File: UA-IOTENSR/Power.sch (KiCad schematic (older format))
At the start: 29 parts, among them J201 ZX62-AB-5PA_31_, J202 S2B-ZR-SM4A-TF(LF)(SN), Q201 2N7002, U201 BQ24196RGER, U202 BD33KA5FP-E2

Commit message: Adding peripherals page
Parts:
- renumbered C211 to C201, C201 to C202, C202 to C203, C212 to C204, C203 to C205, C204 to C206, C205 to C207, C206 to C208, C207 to C209, C208 to C210, C209 to C211, C210 to C212, R207 to R205, R208 to R206, R206 to R207, R205 to R208, U202 to U201, U201 to U202
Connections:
- net labels removed: NoConn
- no-connect marks 0 -> 2
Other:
- moved on the sheet: C201, C202, C203, C204, C205, C206, C207, C208, C209, C210, C211, C212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

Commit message: updated symbols; changed vdd to 3v3 global for pcb design later
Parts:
- removed R202: 10k, symbol Device:R_Small_US
- added R2: 10k, symbol Device:R_Small_US
- D1: renamed from D201; symbol Samacs:PRTR5V0U2X,215 -> UA-IOTENSR-rescue:PRTR5V0U2X,215-Samacs
- J1: renamed from J201; symbol Samacs:ZX62-AB-5PA_31_ -> UA-IOTENSR-rescue:ZX62-AB-5PA_31_-Samacs
- renumbered C201 to C1, C210 to C10, C211 to C11, C212 to C12, C202 to C2, C203 to C3, C204 to C4, C205 to C5, C206 to C6, C207 to C7, C208 to C8, C209 to C9, D202 to D2, D203 to D3, J202 to J2, L201 to L1, Q201 to Q1, R201 to R1, R203 to R3, R204 to R4, R205 to R5, R206 to R6, R207 to R7, R208 to R8, U201 to U2, U202 to U3
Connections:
- net labels added: +5V
- net labels removed: VDD
- wire segments 91 -> 97
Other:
- moved on the sheet: C10

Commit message: Organized PMIC schem
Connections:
- wire segments 97 -> 101
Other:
- note added: "BQ24196 PMIC BATTERY CHARGING CCT"
- note added: "MicroUSB HEADER and TVS DIODE ARRAY IC"
- moved on the sheet: C1, C10, C11, C12, C2, C3, C4, C5, C6, C7, C8, C9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

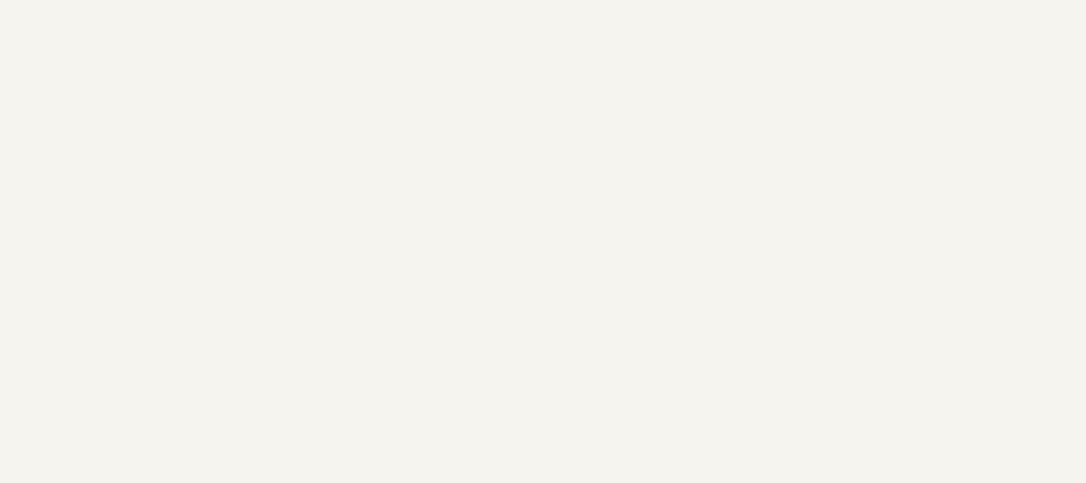
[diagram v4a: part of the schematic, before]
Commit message: Organized ESP32 main schem
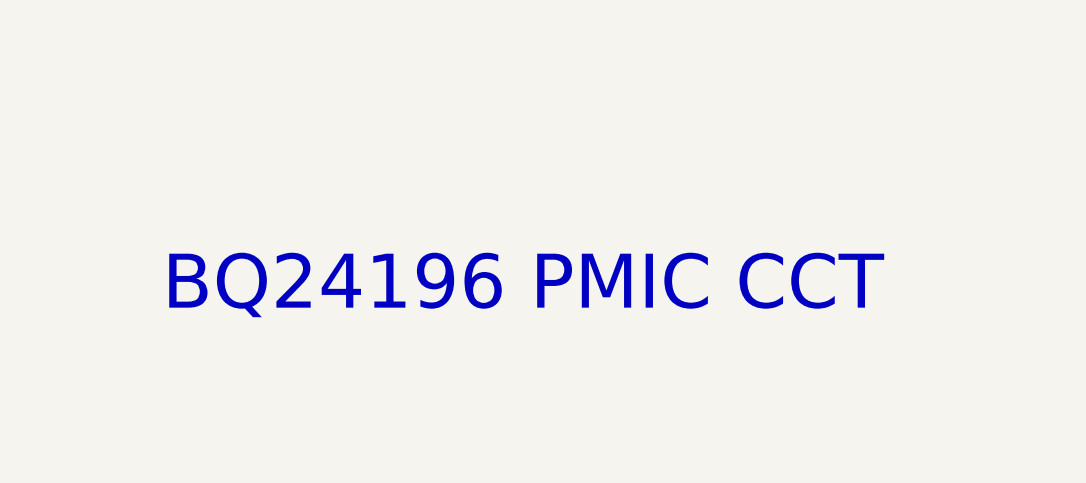
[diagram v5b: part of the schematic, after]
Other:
- note added: "BQ24196 PMIC CCT"
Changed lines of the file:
@@
 Text Notes 6450 5200 0    118  ~ 0
 BQ24196 PMIC BATTERY CHARGING CCT
+Text Notes 7000 7100 0    236  ~ 0
+BQ24196 PMIC CCT
 $EndSCHEMATC

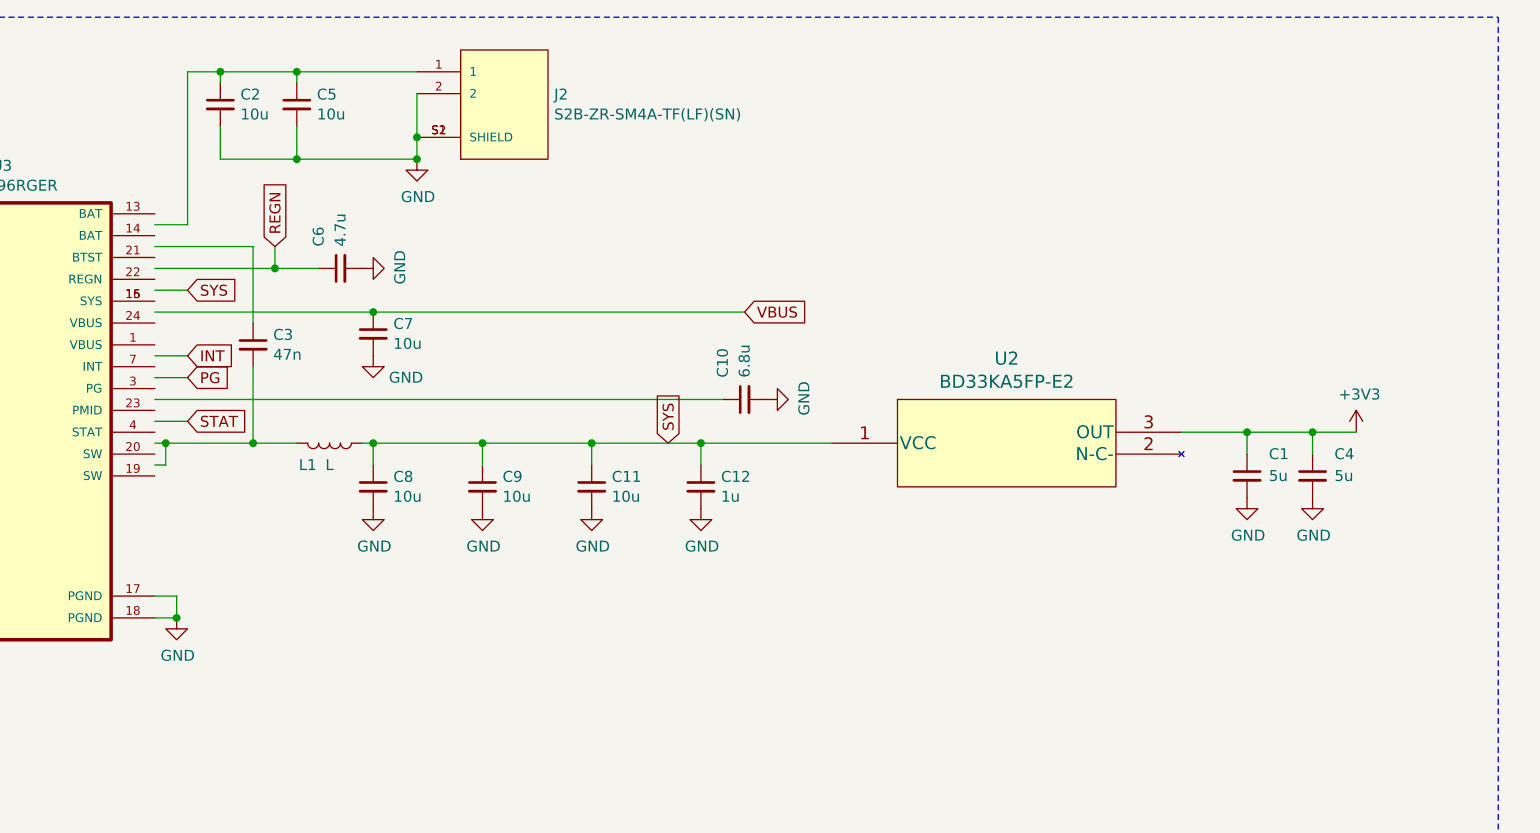
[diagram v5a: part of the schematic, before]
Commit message: Reassessed components
Removed bar graph led array and lm3914
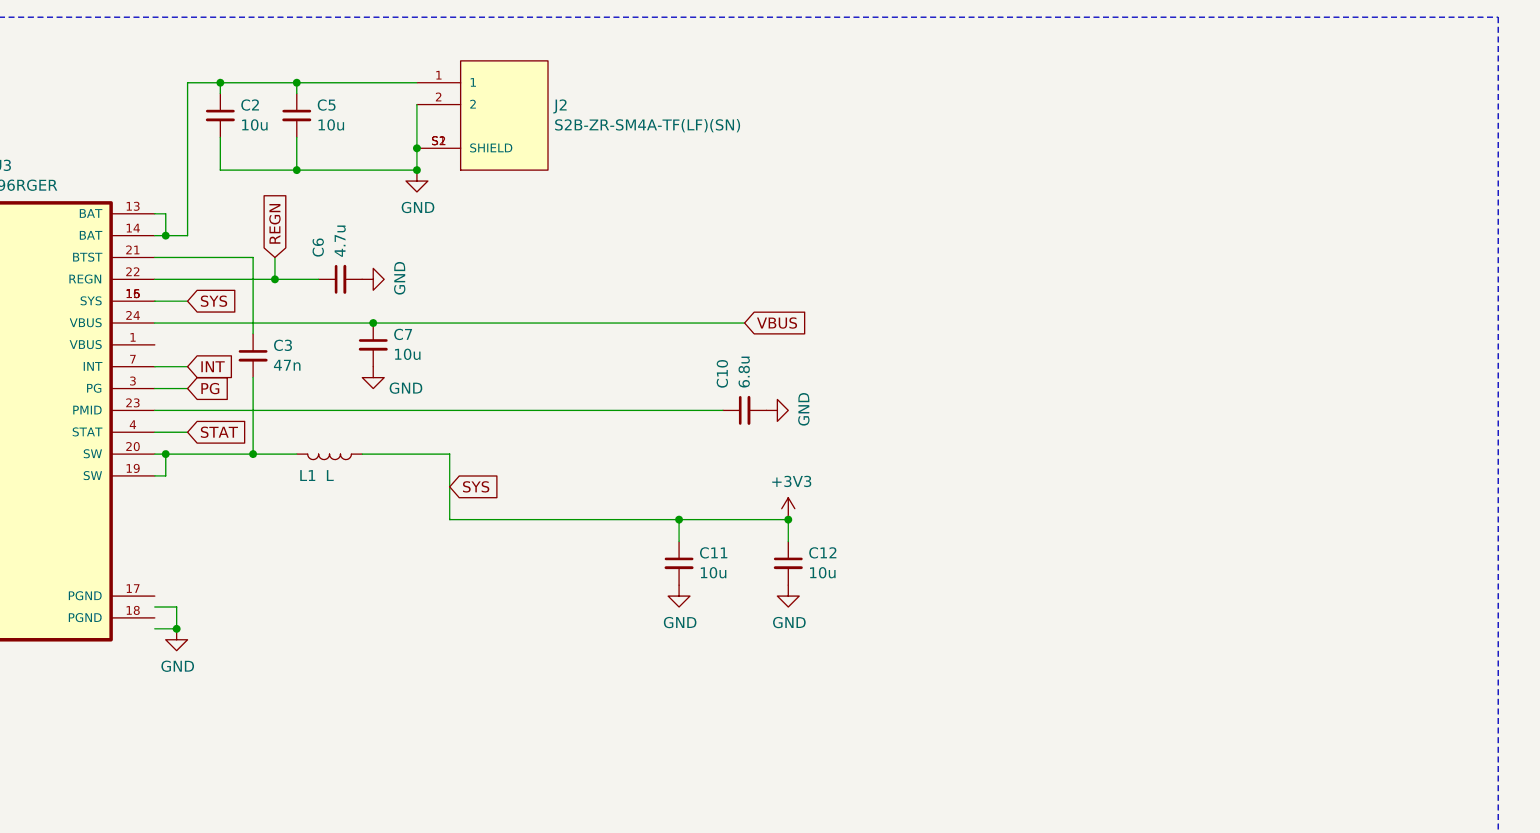
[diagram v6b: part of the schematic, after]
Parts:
- removed C1, C4: 5u, symbol Device:C_Small
- removed C8, C9: 10u, symbol Device:C_Small
- removed U2: BD33KA5FP-E2, TO252-3_ROM, symbol VoltReg:BD33KA5FP-E2
- C12: value 1u -> 10u
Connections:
- wire segments 101 -> 96
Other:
- moved on the sheet: C10, C11, C12, C2, C3, C5, C6, C7, J2, L1

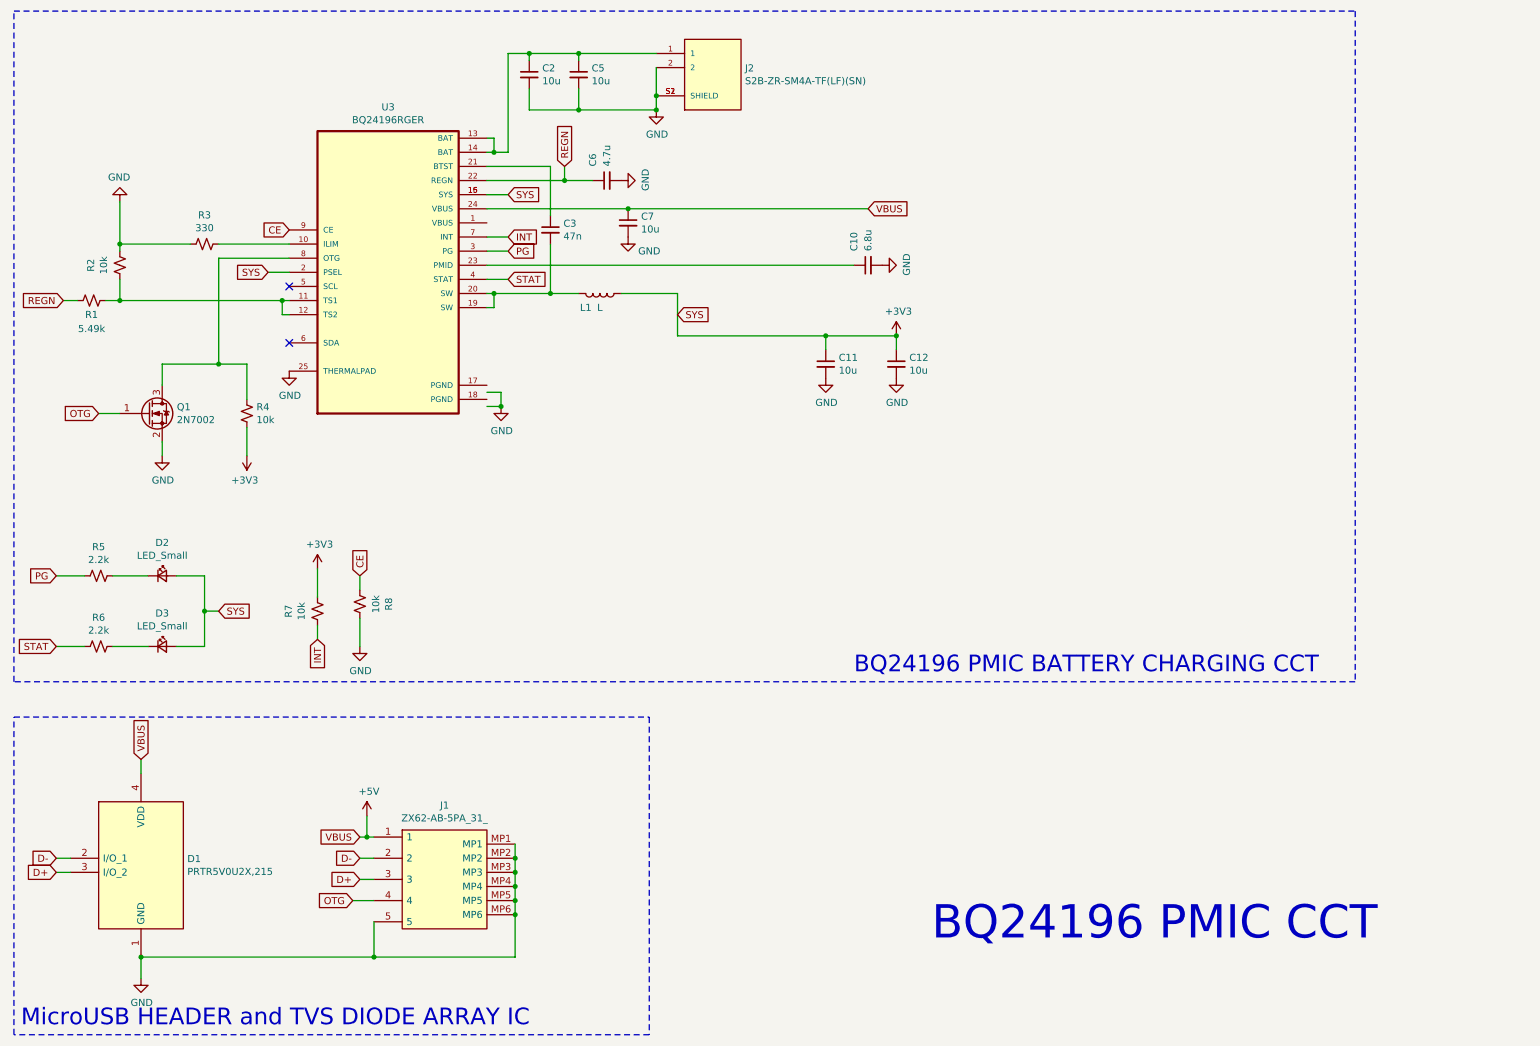
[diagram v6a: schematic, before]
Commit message: Reworking Power Schematic page for the change to NiMH tech
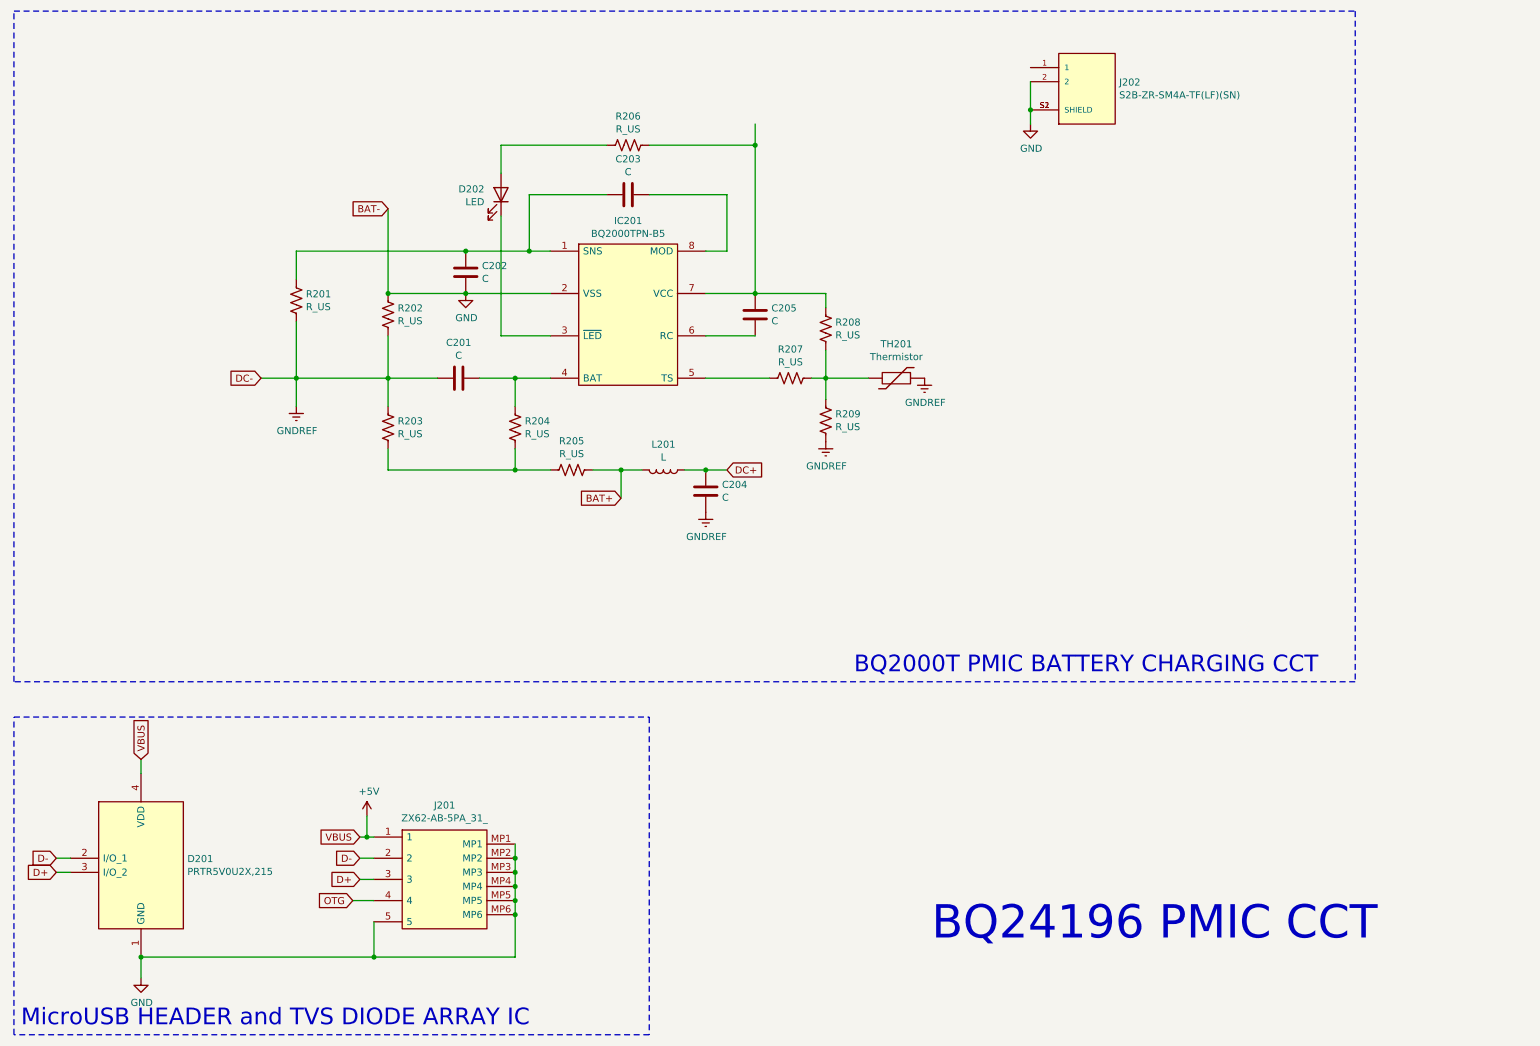
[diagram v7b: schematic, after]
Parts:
- removed C10: 6.8u, symbol Device:C_Small
- removed C11, C12, C2, C5, C7: 10u, symbol Device:C_Small
- removed C3: 47n, symbol Device:C_Small
- removed C6: 4.7u, symbol Device:C_Small
- removed D2, D3: LED_Small, symbol Device:LED_Small
- removed L1: L, symbol Device:L
- removed Q1: 2N7002, Package_TO_SOT_SMD:SOT-23, symbol Transistor_FET:2N7002
- removed R1: 5.49k, symbol Device:R_Small_US
- removed R2, R4, R7, R8: 10k, symbol Device:R_Small_US
- removed R3: 330, symbol Device:R_Small_US
- removed R5, R6: 2.2k, symbol Device:R_Small_US
- removed U3: BQ24196RGER, QFN50P400X400X100-25N, symbol PMIC:BQ24196RGER
- added C201, C202, C203, C204, C205: C, symbol Device:C
- added D202: LED, symbol Device:LED
- added IC201: BQ2000TPN-B5, DIP794W53P254L959H508Q8N, symbol Samacs:BQ2000TPN-B5
- added L201: L, symbol Device:L
- added R201, R202, R203, R204, R205, R206, R207, R208, R209: R_US, symbol Device:R_US
- added TH201: Thermistor, symbol Device:Thermistor
- renumbered D1 to D201, J1 to J201, J2 to J202
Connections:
- net GND: now also C202.2, IC201.2 (VSS), R202.1
- new net: C202.1, C203.2, IC201.1 (SNS), R201.1
- new net: D202.1 (K), IC201.3 (~LED)
- new net: C201.1, IC201.4 (BAT), R204.1
- new net: IC201.5 (TS), R207.2
- new net: C205.2, IC201.6 (RC)
- new net: C205.1, IC201.7 (VCC), R206.1, R208.1
- new net: C203.1, IC201.8 (MOD)
- new net: R203.2, R204.2, R205.2
- new net: D202.2 (A), R206.2
- new net: R207.1, R208.2, R209.1, TH201.2
- new net BAT+: L201.2, R205.1
- new net DC+: C204.1, L201.1
- new net GNDREF: C201.2, C204.2, R201.2, R202.2, R203.1, R209.2, TH201.1
- no-connect marks 2 -> 0
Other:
- note added: "BQ2000T PMIC BATTERY CHARGING CCT"
- note removed: "BQ24196 PMIC BATTERY CHARGING CCT"
- moved on the sheet: J202
